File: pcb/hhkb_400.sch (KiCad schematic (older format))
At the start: 150 parts, among them J1 USB_mini_micro_B, SW1 SW_PUSH, U1 ATMEGA32U4, X1 XTAL_GND

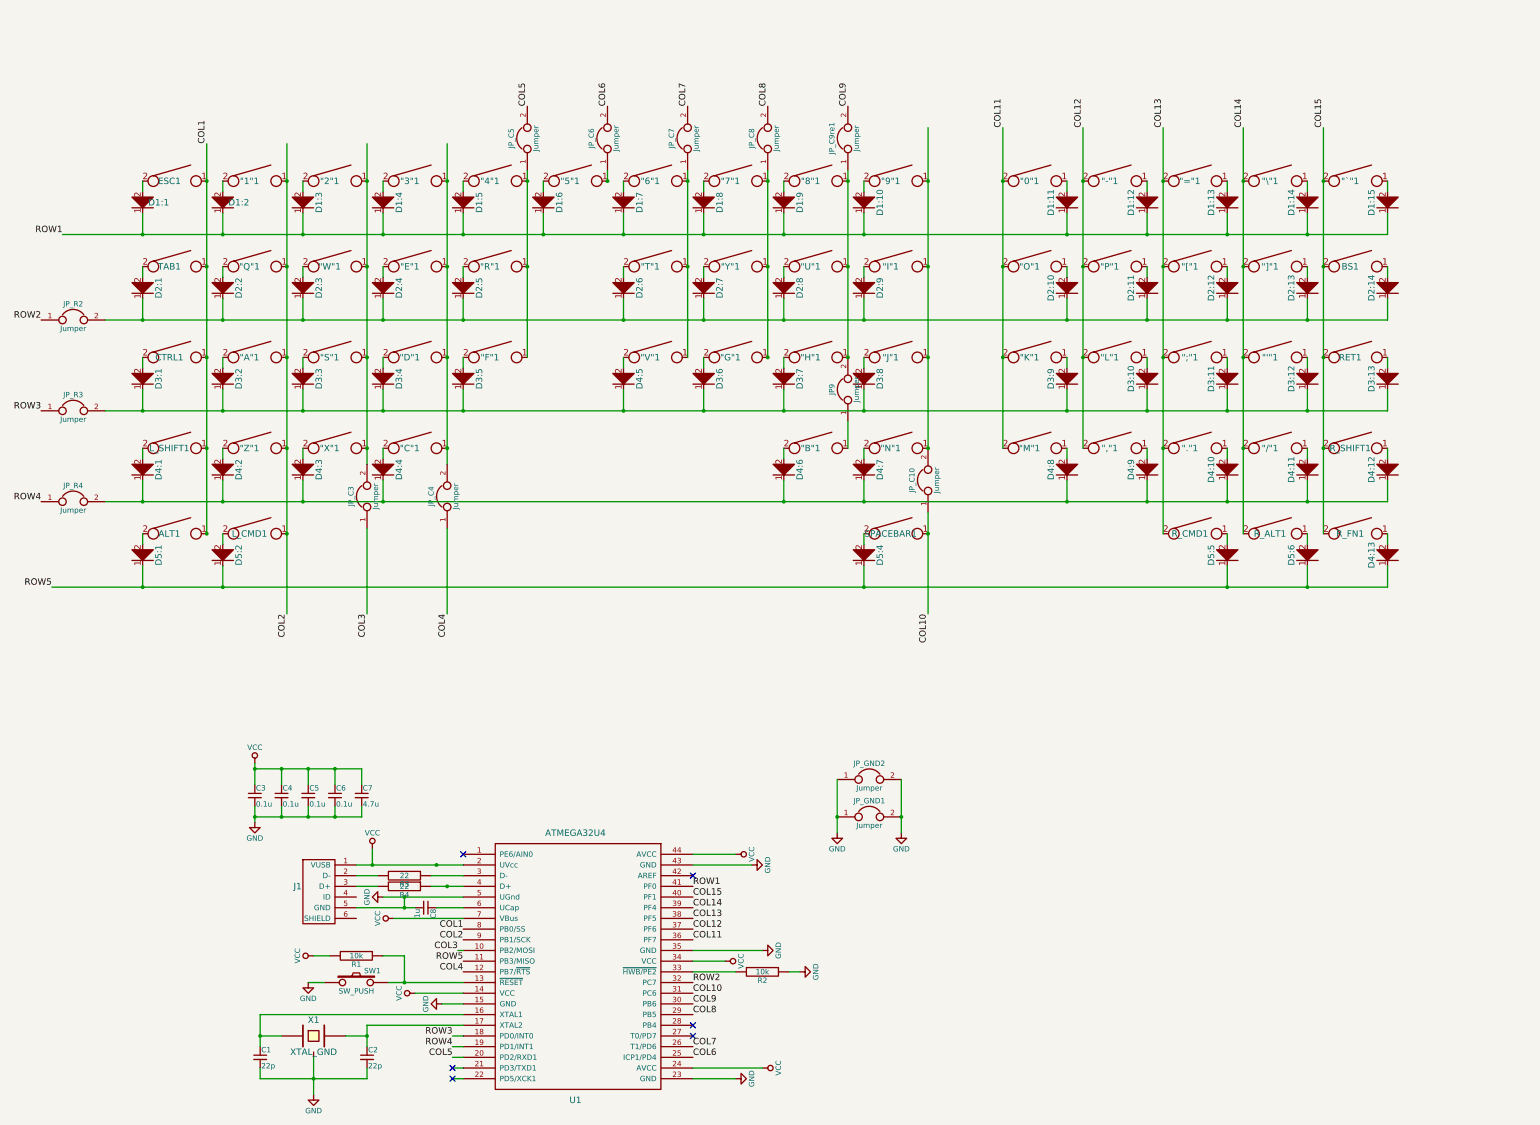
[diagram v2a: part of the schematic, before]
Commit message: rework pcb artwork
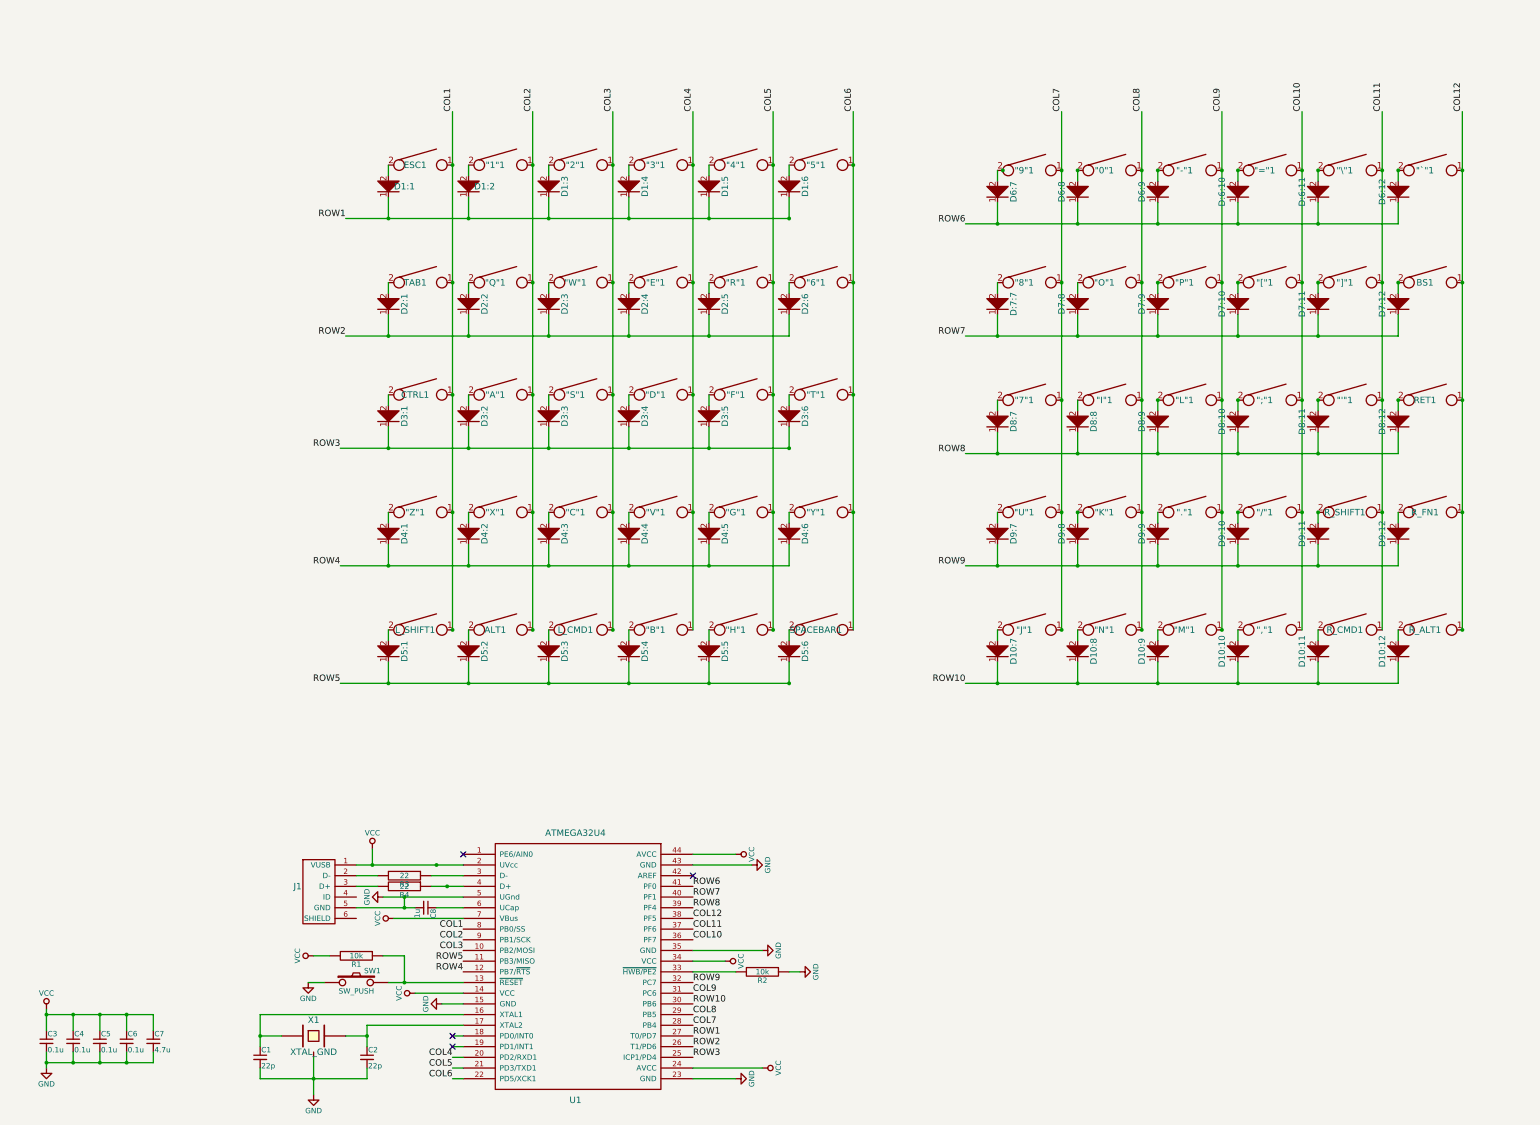
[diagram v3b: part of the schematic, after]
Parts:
- removed JP9, JP_C10, JP_C3, JP_C4, JP_C5, JP_C6, JP_C7, JP_C8, JP_C9re1, JP_GND1, JP_GND2, JP_R2, JP_R3, JP_R4: Jumper, Resistors_SMD:R_1206_HandSoldering, symbol Jumper
- SPACEBAR1: footprint TheKeebrary:MX_Plate_400H -> TheKeebrary:MX_Plate_600H_Stepped
- renumbered D4:9 to D10:10, D5:5 to D10:11, D5:6 to D10:12, D3:8 to D10:7, D4:7 to D10:8, D4:8 to D10:9, D1:7 to D2:6, D2:6 to D3:6, D4:2 to D4:1, D4:3 to D4:2, D4:4 to D4:3, D4:5 to D4:4, D3:6 to D4:5, D2:7 to D4:6, D4:1 to D5:1, D5:1 to D5:2, D5:2 to D5:3, D4:6 to D5:4, D3:7 to D5:5, D5:4 to D5:6, D1:15 to D6:12, D1:10 to D6:7, D1:11 to D6:8, D1:12 to D6:9, D2:12 to D7:10, D2:13 to D7:11, D2:14 to D7:12, D2:10 to D7:8, D2:11 to D7:9, D3:11 to D8:10, D3:12 to D8:11, D3:13 to D8:12, D1:8 to D8:7, D2:9 to D8:8, D3:10 to D8:9, D4:11 to D9:10, D4:12 to D9:11, D4:13 to D9:12, D2:8 to D9:7, D3:9 to D9:8, D4:10 to D9:9, D1:13 to D:6:10, D1:14 to D:6:11, D1:9 to D:7:7
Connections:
- net COL1: now also "Z"1.1; no longer ALT1.1
- net COL10: now also ","1.1, "/"1.1, ";"1.1, "="1.1, "["1.1, U1.36 (PF7); no longer SPACEBAR1.1, U1.31 (PC6)
- net COL11: now also "'"1.1, "\"1.1, "]"1.1, R_CMD1.1, R_SHIFT1.1, U1.37 (PF6); no longer "0"1.2, "K"1.2, "M"1.2, "O"1.2, U1.36 (PF7)
- net COL12: now also "`"1.1, BS1.1, RET1.1, R_ALT1.1, R_FN1.1, U1.38 (PF5); no longer ","1.2, "-"1.2, "L"1.2, "P"1.2, U1.37 (PF6)
- net COL2: now also "X"1.1, ALT1.1; no longer "Z"1.1, L_CMD1.1
- net COL3: now also "2"1.1, "C"1.1, "S"1.1, "W"1.1, L_CMD1.1
- net COL4: now also "3"1.1, "B"1.1, "D"1.1, "E"1.1, "V"1.1, U1.20 (PD2/RXD1); no longer U1.12 (PB7/~RTS)
- net COL5: now also "4"1.1, "F"1.1, "G"1.1, "H"1.1, "R"1.1, U1.21 (PD3/TXD1); no longer U1.20 (PD2/RXD1)
- net COL6: now also "5"1.1, "6"1.1, "T"1.1, "Y"1.1, SPACEBAR1.1, U1.22 (PD5/XCK1); no longer U1.25 (ICP1/PD4)
- net COL7: now also "7"1.1, "8"1.1, "9"1.1, "J"1.1, "U"1.1, U1.28 (PB4); no longer U1.26 (T1/PD6)
- net COL8: now also "0"1.1, "I"1.1, "K"1.1, "N"1.1, "O"1.1
- net COL9: now also "-"1.1, "."1.1, "L"1.1, "M"1.1, "P"1.1, U1.31 (PC6); no longer U1.30 (PB6)
- net ROW1: now also U1.27 (T0/PD7); no longer D2:6.1, D6:12.1, D6:7.1, D6:8.1, D6:9.1, D8:7.1, D:6:10.1, D:6:11.1, D:7:7.1, U1.41 (PF0)
- net ROW2: now also D2:1.1, D2:2.1, D2:3.1, D2:4.1, D2:5.1, D2:6.1, U1.26 (T1/PD6); no longer U1.32 (PC7)
- net ROW3: now also D3:1.1, D3:2.1, D3:3.1, D3:4.1, D3:5.1, D3:6.1, U1.25 (ICP1/PD4); no longer U1.18 (PD0/INT0)
- net ROW4: now also D4:1.1, D4:2.1, D4:3.1, D4:4.1, D4:5.1, D4:6.1, U1.12 (PB7/~RTS); no longer U1.19 (PD1/INT1)
- net ROW5: now also D5:1.1, D5:4.1, D5:5.1; no longer D10:11.1, D10:12.1, D9:12.1
- net at D6:8.2: now also "0"1.2; no longer "0"1.1
- net at D6:9.2: now also "-"1.2; no longer "-"1.1
- net at D:6:10.2: now also "="1.2; no longer "="1.1
- net at D:6:11.2: now also "\"1.2; no longer "\"1.1
- net at D6:12.2: now also "`"1.2; no longer "`"1.1
- net at D7:8.2: now also "O"1.2; no longer "O"1.1
- net at D7:9.2: now also "P"1.2; no longer "P"1.1
- net at D7:10.2: now also "["1.2; no longer "["1.1
- net at D7:11.2: now also "]"1.2; no longer "]"1.1
- net at D7:12.2: now also BS1.2; no longer BS1.1
- net at D9:8.2: now also "K"1.2; no longer "K"1.1
- net at D8:9.2: now also "L"1.2; no longer "L"1.1
- net at D8:10.2: now also ";"1.2; no longer ";"1.1
- net at D8:11.2: now also "'"1.2; no longer "'"1.1
- net at D8:12.2: now also RET1.2; no longer RET1.1
- net at D10:9.2: now also "M"1.2; no longer "M"1.1
- net at D10:10.2: now also ","1.2; no longer ","1.1
- net at D9:9.2: now also "."1.2; no longer "."1.1
- net at D9:10.2: now also "/"1.2; no longer "/"1.1
- net at D9:11.2: now also R_SHIFT1.2; no longer R_SHIFT1.1
- net at D9:12.2: now also R_FN1.2; no longer R_FN1.1
- net at D10:11.2: now also R_CMD1.2; no longer R_CMD1.1
- net at D10:12.2: now also R_ALT1.2; no longer R_ALT1.1
- removed net COL13: "."1.2, ";"1.2, "="1.2, "["1.2, R_CMD1.2, U1.38 (PF5)
- removed net COL14: "'"1.2, "/"1.2, "\"1.2, "]"1.2, R_ALT1.2, U1.39 (PF4)
- removed net COL15: "`"1.2, BS1.2, RET1.2, R_FN1.2, R_SHIFT1.2, U1.40 (PF1)
- new net ROW10: D10:10.1, D10:11.1, D10:12.1, D10:7.1, D10:8.1, D10:9.1, U1.30 (PB6)
- new net ROW6: D6:12.1, D6:7.1, D6:8.1, D6:9.1, D:6:10.1, D:6:11.1, U1.41 (PF0)
- new net ROW7: D7:10.1, D7:11.1, D7:12.1, D7:8.1, D7:9.1, D:7:7.1, U1.40 (PF1)
- new net ROW8: D8:10.1, D8:11.1, D8:12.1, D8:7.1, D8:8.1, D8:9.1, U1.39 (PF4)
- new net ROW9: D9:10.1, D9:11.1, D9:12.1, D9:7.1, D9:8.1, D9:9.1, U1.32 (PC7)
- no-connect marks 7 -> 5
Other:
- moved on the sheet: "'"1, ","1, "-"1, "."1, "/"1, "0"1, "1"1, "2"1, "3"1, "4"1, "5"1, "6"1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
